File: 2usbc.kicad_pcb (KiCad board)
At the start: 4 copper layers, 26 x 30 mm, 51 parts, among them J101 USB_C_Plug_USB2.0, J102 USB_C_Receptacle_USB2.0, J103 USB_C_Receptacle_USB2.0, U101 TLV76733DRVx, U102 USBLC6-2SC6, U201 USB2512B, U301 USBLC6-2SC6, U302 MIC2097-1YMT-TR, U401 USBLC6-2SC6, U402 MIC2097-1YMT-TR, Y201 24MHz

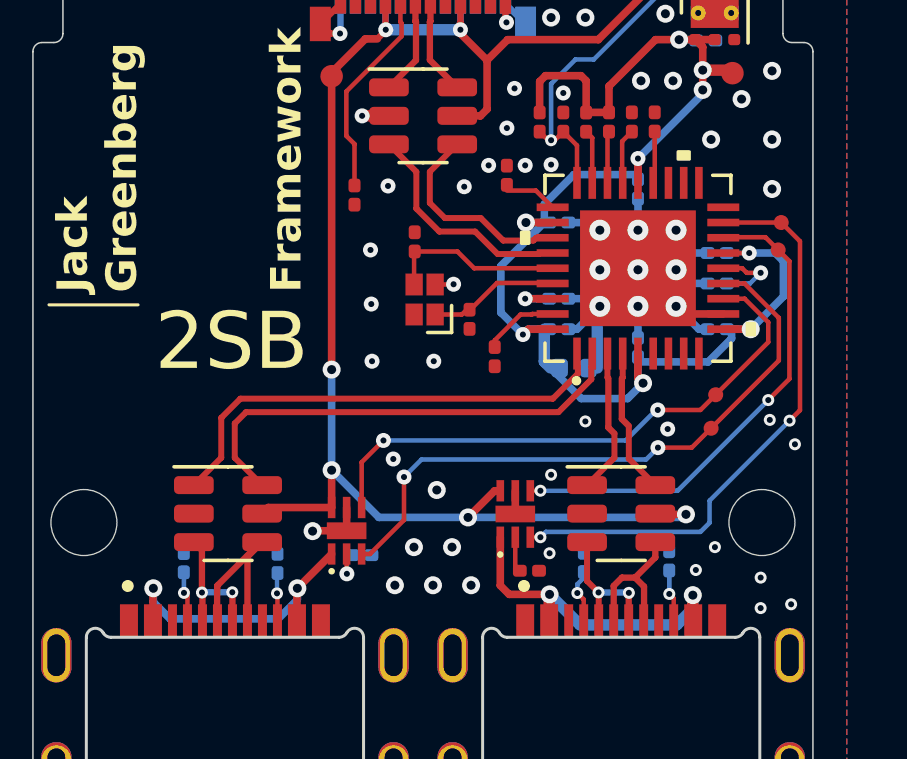
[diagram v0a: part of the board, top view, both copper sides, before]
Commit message: Update CC resistors with feedback
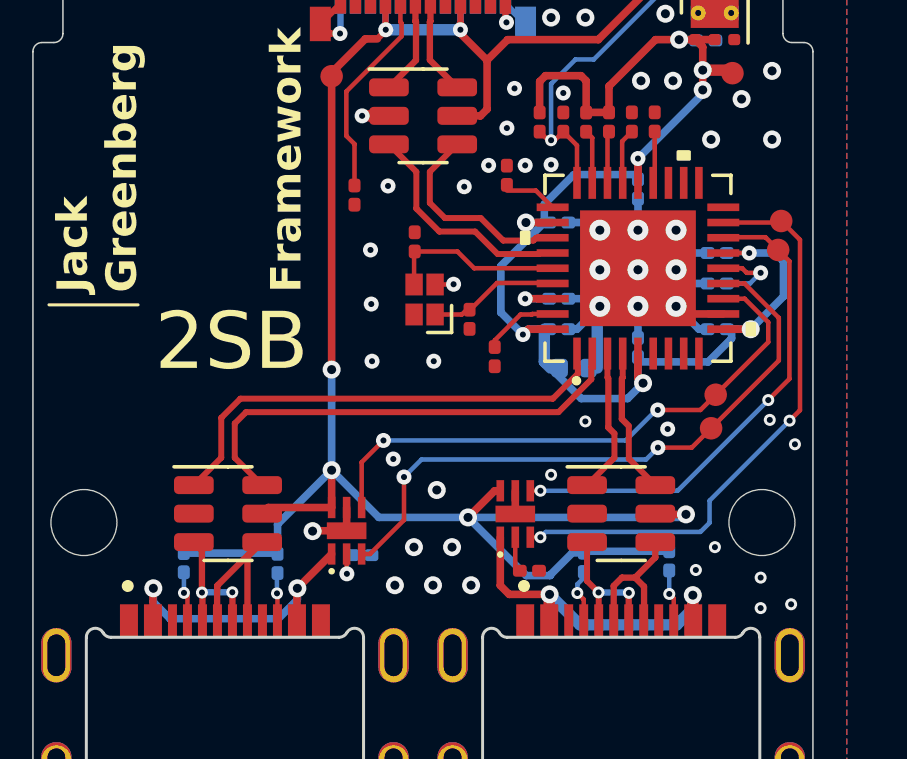
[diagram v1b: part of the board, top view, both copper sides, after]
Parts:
- TP301, TP302, TP401, TP402: footprint 2usb:TestPoint_SM -> 2usb:TestPoint_MD
- moved TP402 0.05 mm to (151.9, 136.4)
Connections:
- R102 pad 2: GND -> VBUS
- R103 pad 2: GND -> VBUS
- R104 pad 2: GND -> VBUS
- R105 pad 2: GND -> VBUS
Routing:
- net VBUS: track 53.8 -> 68.3 mm
- net GND: vias 63 -> 61

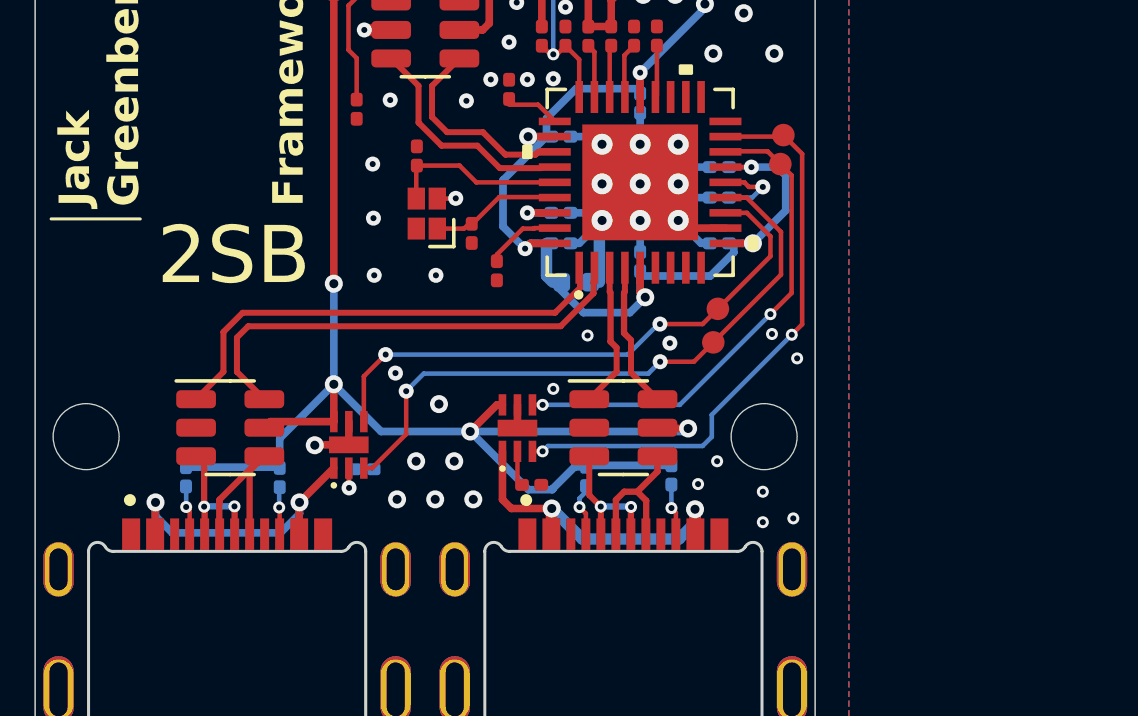
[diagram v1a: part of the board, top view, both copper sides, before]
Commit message: Add power switch ic and channel config ic
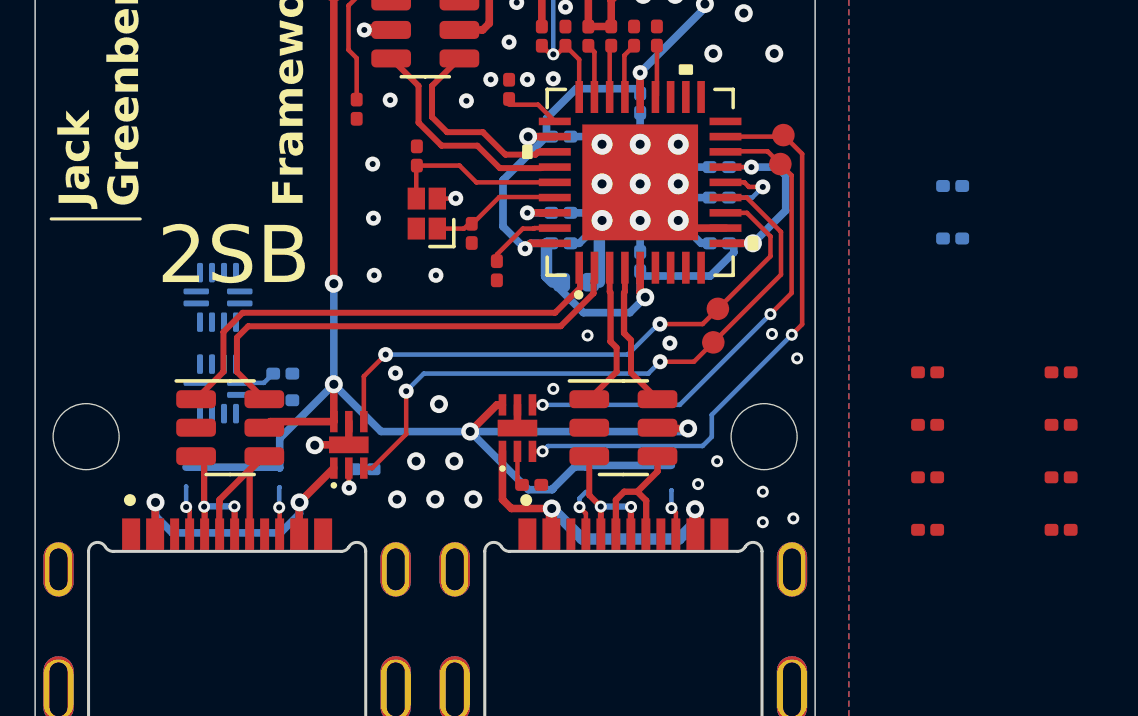
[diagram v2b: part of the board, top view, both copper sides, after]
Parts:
- removed R102, R103, R104, R105: 5.1K, Resistor_SMD:R_0201_0603Metric
- added C301: 0.1uF, Capacitor_SMD:C_0201_0603Metric, F.Cu at (156.7, 144.4)
- added C302: 0.1uF, Capacitor_SMD:C_0201_0603Metric, F.Cu at (156.7, 146.1)
- added C401: 0.1uF, Capacitor_SMD:C_0201_0603Metric, F.Cu at (161.2, 144.4)
- added C402: 0.1uF, Capacitor_SMD:C_0201_0603Metric, F.Cu at (161.2, 146.1)
- added R302: 56K, Resistor_SMD:R_0201_0603Metric, B.Cu at (157.6, 138.1)
- added R303: 56K, Resistor_SMD:R_0201_0603Metric, B.Cu at (157.6, 139.9)
- added R304: 900k, Resistor_SMD:R_0201_0603Metric, F.Cu at (156.7, 147.9)
- added R305: 100K, Resistor_SMD:R_0201_0603Metric, F.Cu at (156.7, 149.6)
- added R402: 56K, Resistor_SMD:R_0201_0603Metric, B.Cu at (135.3, 144.4)
- added R403: 56K, Resistor_SMD:R_0201_0603Metric, B.Cu at (135.3, 145.3)
- added R404: 900k, Resistor_SMD:R_0201_0603Metric, F.Cu at (161.2, 147.9)
- added R405: 100K, Resistor_SMD:R_0201_0603Metric, F.Cu at (161.2, 149.6)
- added U303: TUSB320, Package_DFN_QFN:Texas_X2QFN-12_1.6x1.6mm_P0.4mm, B.Cu at (133.1, 141.9)
- added U403: TUSB320, Package_DFN_QFN:Texas_X2QFN-12_1.6x1.6mm_P0.4mm, B.Cu at (133.1, 144.9)
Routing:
- net /Output Stage 2/CC1: track 0.00 -> 1.24 mm
- net /Output Stage 2/CC2: track 0.00 -> 1.19 mm

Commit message: Layout checkpoint
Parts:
- added C303: 10uF, Capacitor_SMD:C_0201_0603Metric, F.Cu at (129.2, 136.4)
- added C304: 1uF, Capacitor_SMD:C_0201_0603Metric, F.Cu at (129.9, 143.1)
- added C305: 0.1uF, Capacitor_SMD:C_0201_0603Metric, F.Cu at (132.9, 137.2)
- added C403: 10uF, Capacitor_SMD:C_0201_0603Metric, F.Cu at (151.0, 139.2)
- added C404: 1uF, Capacitor_SMD:C_0201_0603Metric, F.Cu at (152.2, 142.9)
- added C405: 0.1uF, Capacitor_SMD:C_0201_0603Metric, F.Cu at (148.0, 143.9)
- added R306: 10K, Resistor_SMD:R_0201_0603Metric, B.Cu at (132.2, 141.8)
- added R406: 10K, Resistor_SMD:R_0201_0603Metric, F.Cu at (149.3, 140.1)
- added U304: AP2161W, 2usb:SON50P181X201X60-7N, F.Cu at (128.3, 142.4)
- added U404: AP2161W, 2usb:SON50P181X201X60-7N, F.Cu at (150.6, 142.2)
- C101, C102, C209, R301: moved to F.Cu
- C301, C401, R101, R201, R202, R203, R204, R205, R206, R207, R208, R305, R401, R405: moved to B.Cu
- R304, R404: value 900k -> 900K; moved to B.Cu
- moved C302 29.4 mm to (127.9, 140.3)
- moved R304 28.2 mm to (128.8, 144.1), turned to 180 degrees
- moved R303 27.8 mm to (130.4, 145.6)
- moved R302 26.7 mm to (131.9, 145.6), turned to 0 degrees
- moved R305 23.9 mm to (133.6, 143.6), turned to 90 degrees
- moved C301 23.5 mm to (133.3, 144.8), turned to 180 degrees
- moved TP106 21.8 mm to (128.7, 129.2)
- moved C102 20.7 mm to (128.9, 127.9), turned to 90 degrees
- moved U101 19.1 mm to (130.7, 128.8), turned to 0 degrees
- moved C101 17.0 mm to (132.5, 127.9), turned to 90 degrees
- moved R404 16.0 mm to (145.6, 143.9), turned to 180 degrees
- moved U403 14.8 mm to (147.9, 143.7), turned to 90 degrees
- moved R402 13.8 mm to (148.9, 146.1)
- moved R405 12.9 mm to (149.7, 143.7), turned to 90 degrees
- moved R301 12.8 mm to (129.2, 138.3), turned to -90 degrees
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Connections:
- net Net-(U303-VBUS_DET) renamed /Output Stage 1/VBUS_DET
- net Net-(U303-~{EN}) renamed /Output Stage 1/~{EN}
- net Net-(U403-VBUS_DET) renamed /Output Stage 2/VBUS_DET
- net Net-(U403-~{EN}) renamed /Output Stage 2/~{EN}
- C302 pad 2: VBUS -> /Output Stage 1/VOUT_I_LIM
- C402 pad 2: VBUS -> /Output Stage 2/VOUT_I_LIM
- R302 pad 1: /Output Stage 1/CC1 -> /P1_CC1
- R303 pad 1: /Output Stage 1/CC2 -> /P1_CC2
- R304 pad 2: VBUS -> /P1_VBUS
- R402 pad 1: /Output Stage 2/CC1 -> /P2_CC1
- R403 pad 1: /Output Stage 2/CC2 -> /P2_CC2
- R404 pad 2: VBUS -> /P2_VBUS
- U302 pad 1: /P1_VBUS -> /Output Stage 1/VOUT_I_LIM
- U303 pad 1: /Output Stage 1/CC1 -> /P1_CC1
- U303 pad 2: /Output Stage 1/CC2 -> /P1_CC2
- U303 pad 9: unconnected-(U303-ID-Pad9) -> /Output Stage 1/ID
- U402 pad 1: /P2_VBUS -> /Output Stage 2/VOUT_I_LIM
- U403 pad 1: /Output Stage 2/CC1 -> /P2_CC1
- U403 pad 2: /Output Stage 2/CC2 -> /P2_CC2
- U403 pad 9: unconnected-(U403-ID-Pad9) -> /Output Stage 2/ID
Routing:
- net +3V3: track 47.3 -> 22.0 mm, vias 9 -> 20
- net GND: track 21.2 -> 38.4 mm, vias 61 -> 46
- net VBUS: track 68.3 -> 56.0 mm, vias 7 -> 10
- net /P2_VBUS: track 11.0 -> 23.0 mm
- net /Hub IC/P2_ENABLE: track 16.6 -> 26.1 mm
- net /P1_VBUS: track 9.97 -> 18.9 mm, vias 2 -> 3
- net /Hub IC/USB_P2_DN: track 4.86 -> 13.4 mm
- net /Hub IC/USB_P2_DP: track 4.86 -> 13.4 mm
- net /P2_CC1: track 1.61 -> 9.20 mm
- net /Output Stage 1/ID: track 0.00 -> 7.50 mm, vias 0 -> 1
- net /P1_CC2: track 1.61 -> 8.75 mm
- net /Hub IC/P1_OVER_CURRENT: track 21.2 -> 27.9 mm
- net /Output Stage 1/OUT_USB_DN: track 4.71 -> 11.3 mm
- net /Output Stage 1/VOUT_I_LIM: track 0.00 -> 6.41 mm
- net /Output Stage 2/VOUT_I_LIM: track 0.00 -> 6.24 mm
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- added copper zone on F.Cu, net +3V3
- added copper zone on In2.Cu, net +3V3
- added copper zone on In2.Cu, net VBUS
- removed copper zone on In2.Cu, net GND
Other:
- board text added: "SIG GND PWR PWR GND SIG"
- board text added: "frame .work"
- board text removed: "Framework"

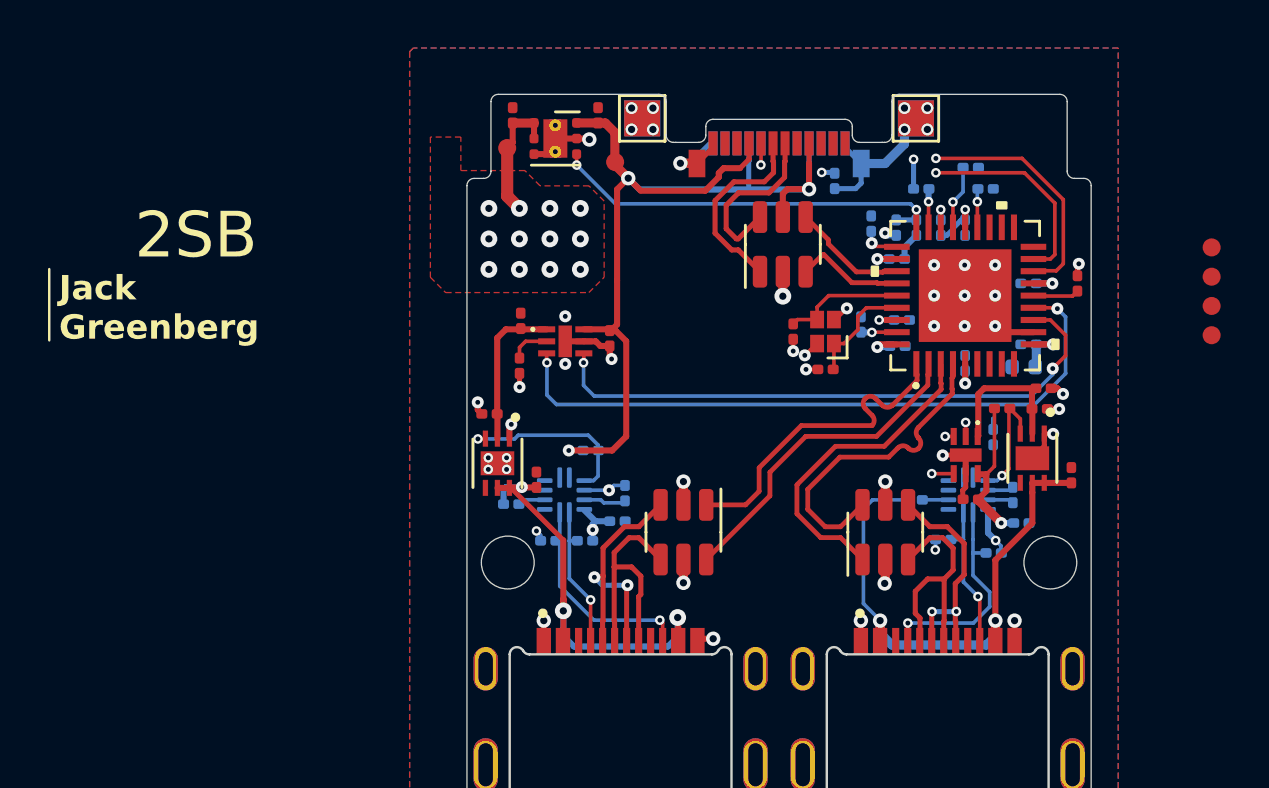
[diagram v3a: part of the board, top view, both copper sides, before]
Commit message: Update layout to be a bit more symmetrical
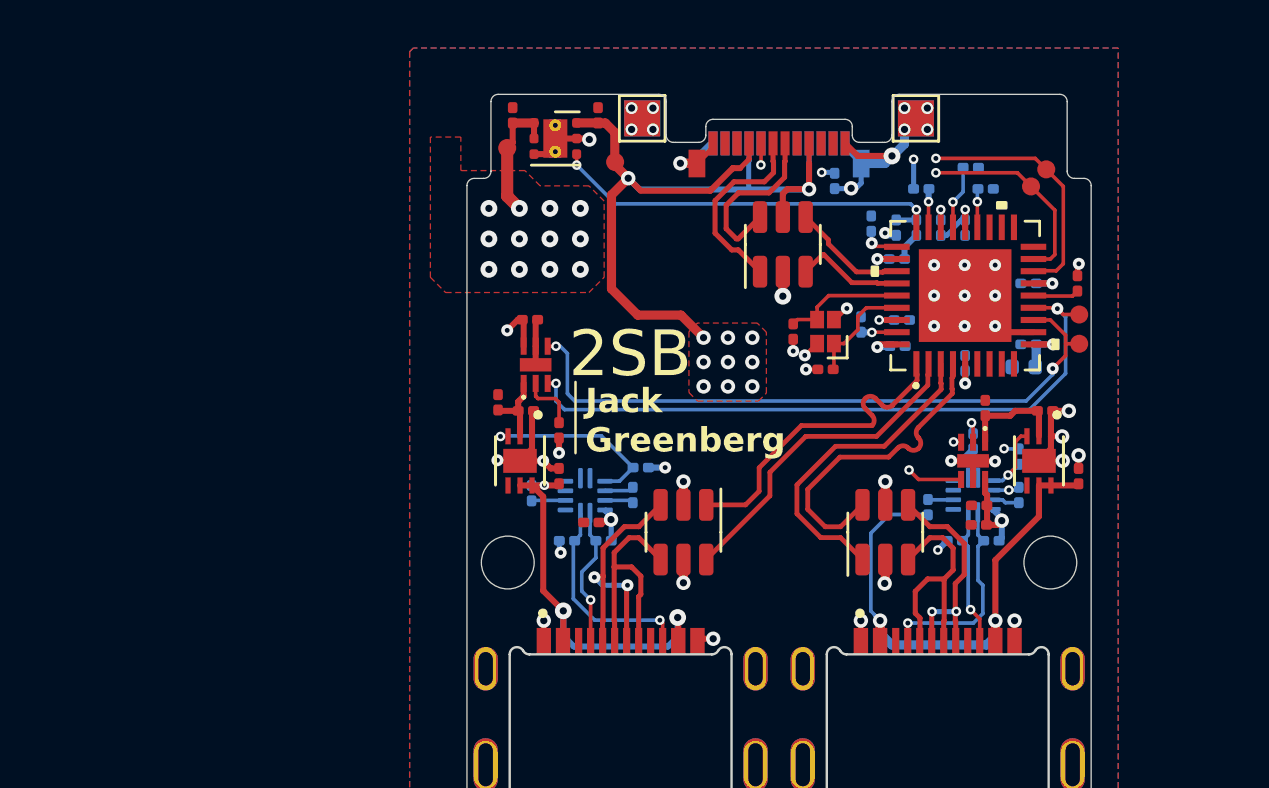
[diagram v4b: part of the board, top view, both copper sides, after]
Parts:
- C301, C401: moved to F.Cu
- R406: moved to B.Cu
- moved TP401 8.21 mm to (151.1, 130.1)
- moved TP402 7.94 mm to (150.5, 130.8)
- moved TP301 5.53 mm to (152.5, 137.4)
- moved TP302 5.53 mm to (152.5, 136.2)
- moved C303 3.75 mm to (129.5, 140.2), turned to 180 degrees
- moved C305 3.41 mm to (129.6, 136.4), turned to 180 degrees
- moved R301 3.16 mm to (130.8, 141.0)
- moved C402 2.27 mm to (148.6, 140.1), turned to -90 degrees
- moved R306 2.20 mm to (134.2, 142.5), turned to 180 degrees
- moved R406 2.12 mm to (150.0, 142.1), turned to -90 degrees
- moved C401 1.77 mm to (148.3, 144.9), turned to 0 degrees
- moved U302 1.57 mm to (129.9, 138.3), turned to 90 degrees
- moved C301 1.09 mm to (132.2, 144.8), turned to 0 degrees
- moved R304 0.96 mm to (129.7, 143.6), turned to 90 degrees
- moved C304 0.95 mm to (130.8, 142.9)
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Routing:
- net VBUS: track 56.0 -> 47.9 mm, vias 10 -> 20
- net GND: track 38.4 -> 46.5 mm, vias 46 -> 43
- net /Output Stage 1/VOUT_I_LIM: track 6.41 -> 3.18 mm
- net /Hub IC/P1_ENABLE: track 24.9 -> 27.4 mm
- net /Output Stage 2/VOUT_I_LIM: track 6.24 -> 4.45 mm
- net /P1_VBUS: track 18.9 -> 17.2 mm
- net /Output Stage 2/ID: track 4.84 -> 3.45 mm
- net /Output Stage 1/ILIMIT: track 1.68 -> 2.46 mm
- net /Hub IC/P2_ENABLE: track 26.1 -> 26.8 mm
- net /P2_CC1: track 9.20 -> 8.54 mm
- net /Output Stage 1/~{EN}: track 1.79 -> 1.20 mm
- added copper zone on F.Cu, net VBUS
